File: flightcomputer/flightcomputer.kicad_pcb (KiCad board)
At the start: 4 copper layers, 299 x 188 mm, 69 parts, among them J1 Conn_Coaxial, J10 Conn_01x03, J11 Conn_01x03, J12 ESQ-113-14-G-D, J2 Conn_Coaxial, J3 Conn_Coaxial, J4 Conn_Coaxial, J5 S3B-PH-K-S-GW, J6 S3B-PH-K-S-GW, J7 S4B-PH-K-S_LF__SN_, J8 S3B-PH-K-S-GW, J9 Conn_01x06, U1 MAX-M10S, U2 LIS2MDLTR, U3 BMI088, U4 MS5607-02BA, U7 Teensy4.1, U8 LSM6DSO32TR, U9 RFM96W-433S2

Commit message: resize
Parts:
- added G***: LOGO, HPRlibrary:HPRLOGOSILK, F.Cu at (237.0, 100.0)
- moved C9 102.5 mm to (40.2, 16.8), turned to 0 degrees
- moved U1 91.9 mm to (40.2, 25.8), turned to -90 degrees
- moved R1 84.6 mm to (45.2, 35.7), turned to 90 degrees
- moved R2 81.8 mm to (42.2, 35.8), turned to -90 degrees
- moved TP3 81.4 mm to (50.2, 17.8), turned to 180 degrees
- moved R7 79.3 mm to (39.6, 36.0), turned to -90 degrees
- moved J2 71.3 mm to (45.2, 44.8), turned to -90 degrees
- moved TP2 69.0 mm to (50.2, 28.8), turned to 180 degrees
- moved BT1 67.7 mm to (44.5, 47.8), turned to 180 degrees
- moved J1 61.7 mm to (35.2, 44.8), turned to -90 degrees
- moved R17 53.1 mm to (20.7, 109.2), turned to 180 degrees
- moved J11 51.2 mm to (61.9, 130.0)
- moved S1 44.4 mm to (19.2, 116.2)
- moved J9 31.7 mm to (145.5, 96.0), turned to -90 degrees
- moved TP1 24.1 mm to (131.0, 121.0), turned to 90 degrees
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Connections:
- J12 pad 01: Net-(J12-Pad01) -> GND
- J12 pad 02: /5V -> Net-(J12-Pad02)
- J12 pad 03: Net-(J12-Pad03) -> GND
- J12 pad 04: /5V -> Net-(J12-Pad04)
- J12 pad 05: /aux7_rx -> GND
- J12 pad 06: /5V -> /aux7_rx
- J12 pad 07: /aux7_tx -> GND
- J12 pad 08: /5V -> /aux7_tx
- J12 pad 09: /can_rx -> GND
- J12 pad 10: /5V -> /can_rx
- J12 pad 11: /can_tx -> GND
- J12 pad 12: /5V -> /can_tx
- J12 pad 13: /SENSE_mosi -> /5V
- J12 pad 14: /5V -> /SENSE_mosi
- J12 pad 15: /SENSE_miso -> /5V
- J12 pad 16: GND -> /SENSE_miso
- J12 pad 17: /SENSE_sck -> /5V
- J12 pad 18: GND -> /SENSE_sck
- J12 pad 19: /servo2_pwm -> /5V
- J12 pad 20: GND -> /servo2_pwm
- J12 pad 21: /servo1_pwm -> /5V
- J12 pad 22: GND -> /servo1_pwm
- J12 pad 23: /PYRO1 -> /5V
- J12 pad 24: GND -> /PYRO1
- J12 pad 25: /PYRO2 -> /5V
- J12 pad 26: GND -> /PYRO2
- R15 pad 1: /teensy_3.3v -> Net-(J12-Pad04)
- R15 pad 2: Net-(J12-Pad03) -> /teensy_3.3v
- R16 pad 1: /teensy_3.3v -> Net-(J12-Pad02)
- R16 pad 2: Net-(J12-Pad01) -> /teensy_3.3v
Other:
- board size 299 x 188 mm -> 130 x 70 mm

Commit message: flight computer routing
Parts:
- removed R16: 0, Resistor_SMD:R_0603_1608Metric_Pad0.98x0.95mm_HandSolder
- removed TP15, TP16, TP17, TP18, TP5, TP6, TP7, TP8: TestPoint, Connector_PinHeader_2.54mm:PinHeader_1x01_P2.54mm_Vertical
- added J14: S3B-PH-K-S-GW, HPRlibrary:S3BPHKSGW, F.Cu at (113.0, 70.5)
- added TP1: TestPoint, Connector_PinHeader_2.54mm:PinHeader_1x01_P2.54mm_Vertical, F.Cu at (109.0, 77.0)
- C9: moved to B.Cu
- J6, J8: value S3B-PH-K-S-GW -> Conn_01x03; footprint HPRlibrary:S3BPHKSGW -> Connector_PinHeader_2.54mm:PinHeader_1x03_P2.54mm_Vertical
- moved C9 112.5 mm to (67.0, 126.0)
- moved BT1 87.2 mm to (63.0, 133.0), turned to 0 degrees
- moved U1 86.7 mm to (56.0, 111.0)
- moved R7 86.0 mm to (55.4, 120.5)
- moved J2 85.5 mm to (52.0, 130.0)
- moved TP3 84.8 mm to (61.9, 101.8)
- moved R1 82.0 mm to (66.0, 115.0)
- moved J1 79.6 mm to (43.0, 124.0), turned to 180 degrees
- moved R2 78.9 mm to (66.0, 111.0)
- moved TP2 73.2 mm to (56.0, 101.8)
- moved J6 53.0 mm to (132.0, 75.5), turned to 0 degrees
- moved J9 41.3 mm to (105.5, 106.0), turned to 90 degrees
- moved J10 37.4 mm to (132.0, 100.5), turned to 0 degrees
- moved C10 36.0 mm to (114.0, 111.0), turned to 0 degrees
- moved J12 35.8 mm to (126.0, 75.0)
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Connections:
- J12 pad 01: GND -> Net-(J12-Pad01)
- J12 pad 02: Net-(J12-Pad02) -> unconnected-(J12-Pad02)
- J12 pad 03: GND -> /servo2_pwm
- J12 pad 04: Net-(J12-Pad04) -> unconnected-(J12-Pad04)
- J12 pad 05: GND -> /servo1_pwm
- J12 pad 06: /aux7_rx -> unconnected-(J12-Pad06)
- J12 pad 08: /aux7_tx -> unconnected-(J12-Pad08)
- J12 pad 10: /can_rx -> unconnected-(J12-Pad10)
- J12 pad 12: /can_tx -> unconnected-(J12-Pad12)
- J12 pad 13: /5V -> GND
- J12 pad 14: /SENSE_mosi -> unconnected-(J12-Pad14)
- J12 pad 15: /5V -> GND
- J12 pad 16: /SENSE_miso -> unconnected-(J12-Pad16)
- J12 pad 17: /5V -> GND
- J12 pad 18: /SENSE_sck -> unconnected-(J12-Pad18)
- J12 pad 20: /servo2_pwm -> unconnected-(J12-Pad20)
- J12 pad 22: /servo1_pwm -> unconnected-(J12-Pad22)
- J12 pad 24: /PYRO1 -> unconnected-(J12-Pad24)
- J12 pad 26: /PYRO2 -> unconnected-(J12-Pad26)
- J6 pad 1: /aux2_tx -> GND
- J6 pad 2: /aux2_rx -> GND
- J8 pad 1: /aux7_tx -> /SENSE_mosi
- J8 pad 2: /aux7_rx -> /SENSE_miso
- J8 pad 3: GND -> /SENSE_sck
- J9 pad 1: /radio_dio5 -> /radio_dio3
- J9 pad 3: /radio_dio3 -> /radio_dio5
- J9 pad 4: /radio_dio2 -> /radio_dio1
- J9 pad 5: /radio_dio1 -> /radio_dio2
- R1 pad 1: /gps_3.3v -> /teensy_3.3v
- R15 pad 1: Net-(J12-Pad04) -> /teensy_3.3v
- R15 pad 2: /teensy_3.3v -> Net-(J12-Pad01)
- R2 pad 1: /gps_3.3v -> /teensy_3.3v
- TP4 pad 1: /SENSE_sck -> /can_rx
- U7 pad 10: /aux2_tx -> /PYRO1CONN
- U7 pad 11: /buzz_pwm -> /radio_reset
- U7 pad 16: /imu_accel_int1 -> /x_fault
- U7 pad 17: /imu_gyro_int1 -> /x_cursns
- U7 pad 20: /aux7_rx -> /lsmimu_int
- U7 pad 21: /aux7_tx -> /lsmimu_cs
- U7 pad 24: /radio_reset -> /buzz_pwm
- U7 pad 25: unconnected-(U7-33_MCLK2-Pad25) -> /imu_gyro_int1
- U7 pad 31: unconnected-(U7-39_MISO1_OUT1A-Pad31) -> /imu_accel_int1
- U7 pad 32: /PYRO1 -> /5v_fault
- U7 pad 33: /PYRO2 -> /5v_cursns
- U7 pad 44: /lsmimu_cs -> /6v_fault
- U7 pad 45: /lsmimu_int -> /6v_cursns
- U7 pad 7: unconnected-(U7-5_IN2-Pad7) -> /PYRO2
- U7 pad 8: unconnected-(U7-6_OUT1D-Pad8) -> /PYRO1
- U7 pad 9: /aux2_rx -> /PYRO2CONN
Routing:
- net /SENSE_sck: track 0.00 -> 80.5 mm
- net /radio_sck: track 0.00 -> 61.7 mm, vias 0 -> 1
- net /radio_reset: track 0.00 -> 58.9 mm, vias 0 -> 1
- net /SENSE_mosi: track 0.00 -> 54.9 mm
- net /SENSE_miso: track 0.00 -> 51.0 mm
- net /buzz_pwm: track 0.00 -> 49.3 mm
- net /imu_gyro_int1: track 0.00 -> 47.1 mm, vias 0 -> 1
- net /radio_mosi: track 0.00 -> 40.5 mm, vias 0 -> 1
- net /teensy_3.3v: track 0.00 -> 40.5 mm, vias 0 -> 1
- net /aux1_sda: track 0.00 -> 37.6 mm
- net /imu_gyro_cs: track 0.00 -> 37.1 mm, vias 0 -> 1
- net /imu_accel_cs: track 0.00 -> 33.1 mm, vias 0 -> 1
- net /radio_cs: track 0.00 -> 30.3 mm
- net /aux8_tx: track 0.00 -> 29.5 mm
- net /aux1_scl: track 0.00 -> 29.0 mm
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- added copper zone on B.Cu, net /gps_vbckp
- added copper zone on F.Cu, net /gps_vbckp
- added copper zone on In2.Cu, net /teensy_3.3v
- added copper zone on B.Cu, net GND
- added copper zone on F.Cu, net GND
- added copper zone on In1.Cu, net GND
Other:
- board size 130 x 70 mm -> 100 x 75 mm
- rule pad_to_mask_clearance: 0 -> 0.1

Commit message: fc checkpoint
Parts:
- moved TP4 12.7 mm to (103.5, 71.5)
- moved TP1 11.9 mm to (103.5, 66.5)
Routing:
- net /radio_mosi: track 40.5 -> 61.0 mm, vias 1 -> 2
- net /teensy_3.3v: track 40.5 -> 53.5 mm, vias 1 -> 6
- net /SENSE_mosi: track 54.9 -> 65.3 mm, vias 0 -> 1
- net GND: track 11.5 -> 17.4 mm, vias 0 -> 11
- net /buzz_pwm: track 49.3 -> 52.4 mm
- net /SENSE_sck: track 80.5 -> 81.4 mm
- added copper zone on In2.Cu, net /5V

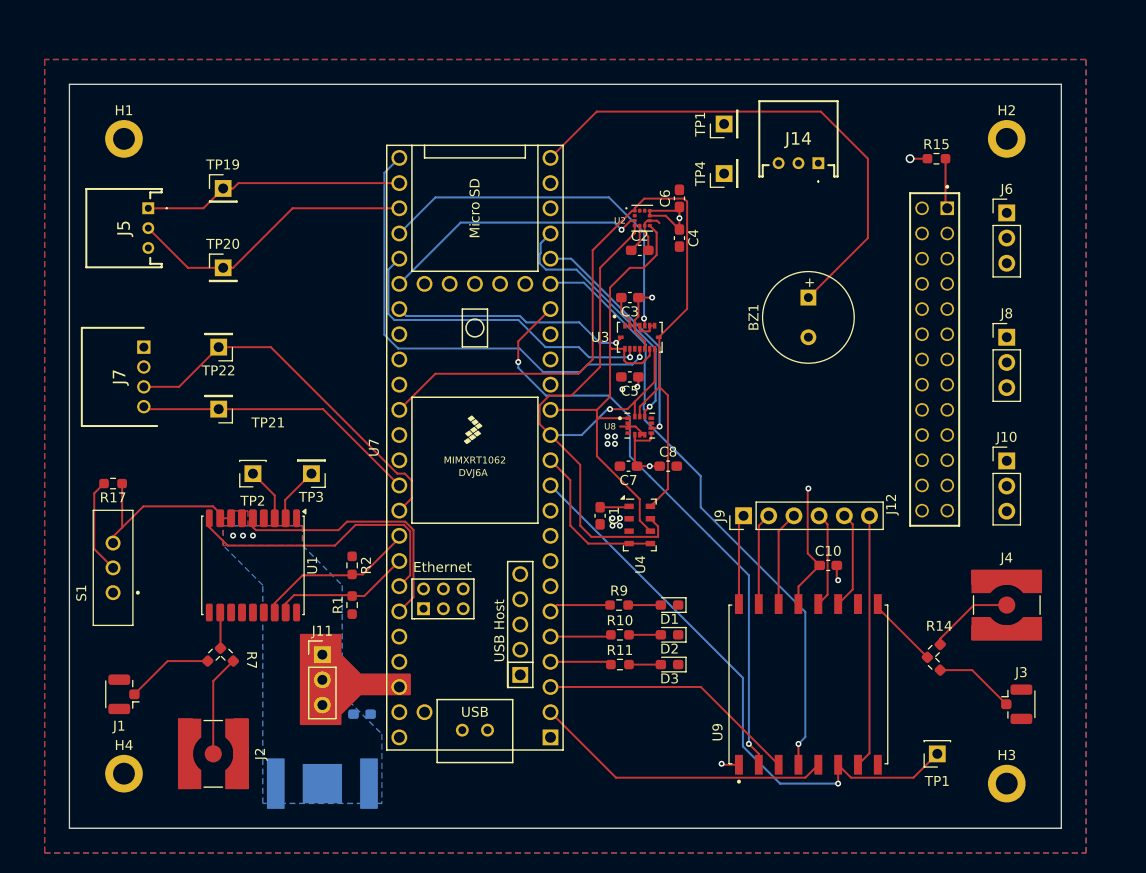
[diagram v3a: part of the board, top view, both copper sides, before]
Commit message: clean up, aligning connectors and board coordinates between fc and power board
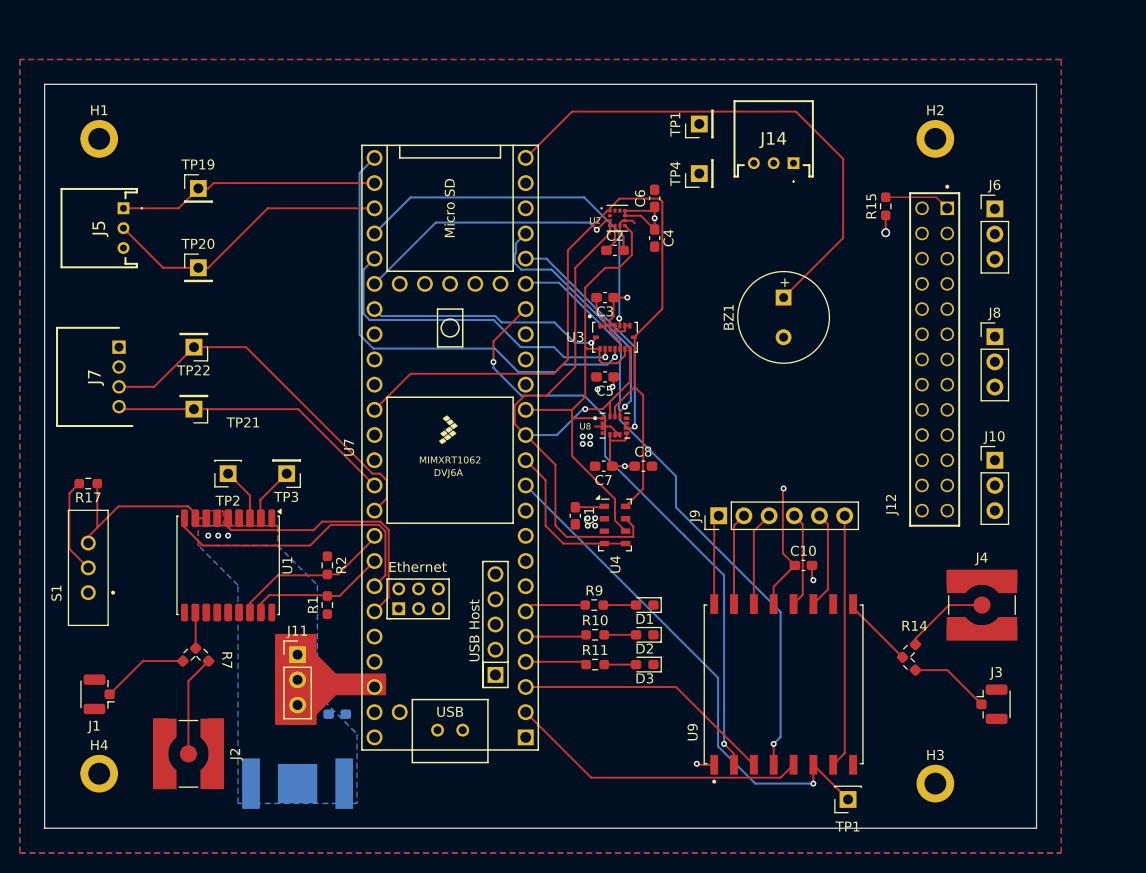
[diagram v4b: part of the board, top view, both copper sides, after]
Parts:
- moved TP1 10.1 mm to (116.0, 134.6)
- moved H2 7.20 mm to (124.8, 68.0)
- moved H3 7.20 mm to (124.8, 133.0)
- moved R15 7.01 mm to (119.8, 74.8), turned to 90 degrees
- moved BT1 2.50 mm to (60.5, 133.0)
- moved BZ1 2.50 mm to (109.5, 84.0)
- moved C1 2.50 mm to (88.5, 106.0)
- moved C10 2.50 mm to (111.5, 111.0)
- moved C2 2.50 mm to (92.5, 79.2)
- moved C3 2.50 mm to (91.5, 84.0)
- moved C4 2.50 mm to (96.5, 78.0)
- moved C5 2.50 mm to (91.5, 92.0)
- moved C6 2.50 mm to (96.5, 74.0)
- moved C7 2.50 mm to (91.4, 101.0)
- moved C8 2.50 mm to (95.4, 101.0)
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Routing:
- net /radio_reset: track 58.9 -> 52.3 mm
- net Net-(J12-Pad01): track 5.07 -> 6.66 mm

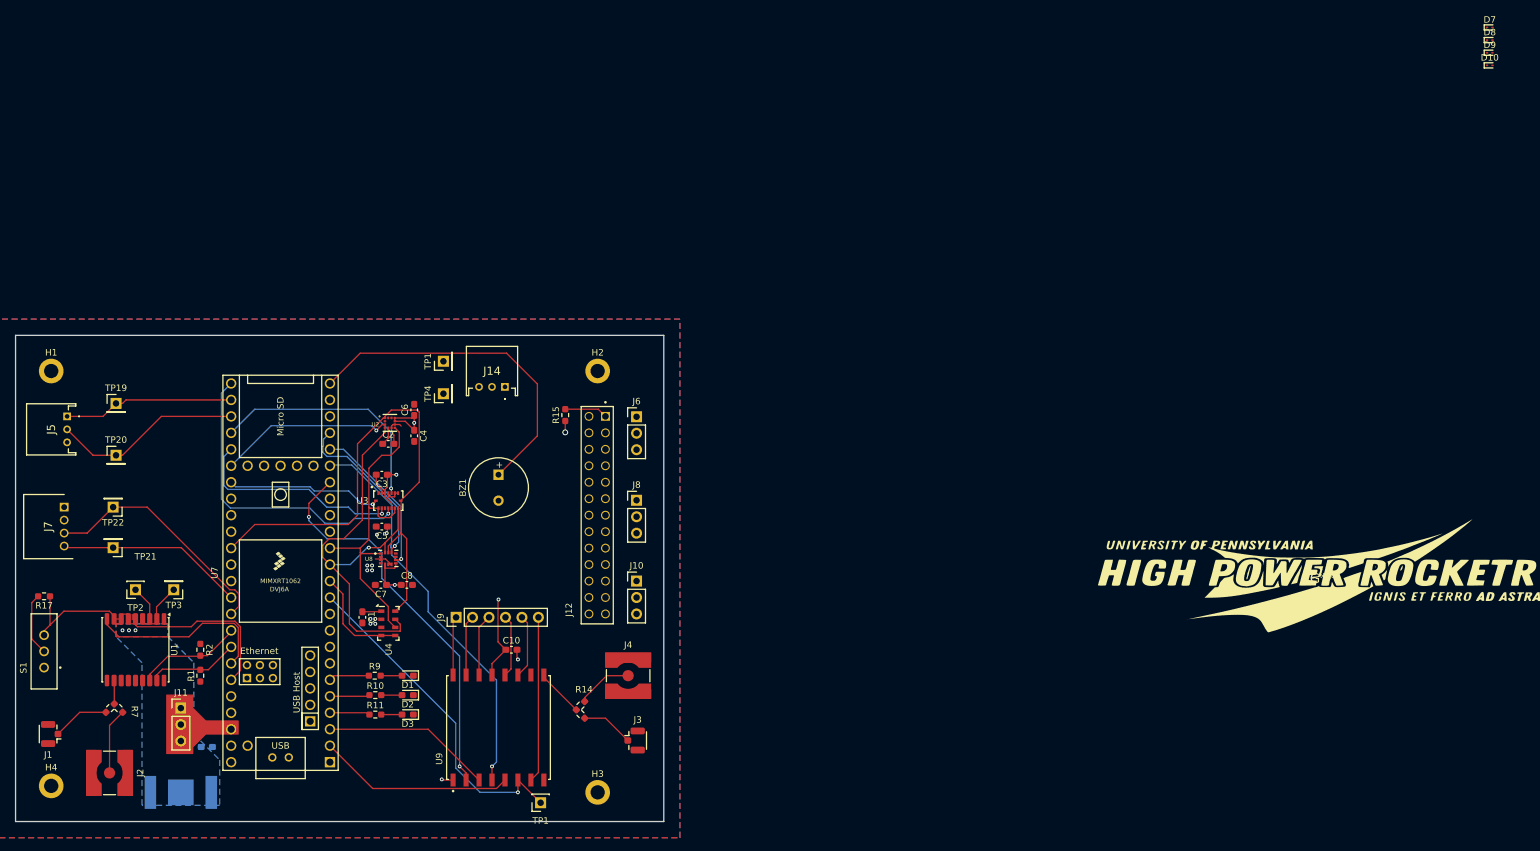
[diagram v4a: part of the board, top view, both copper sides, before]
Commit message: hole+connector alignment finish, fc signal routing finish, fc drc warnings related to footprints/silkscreen
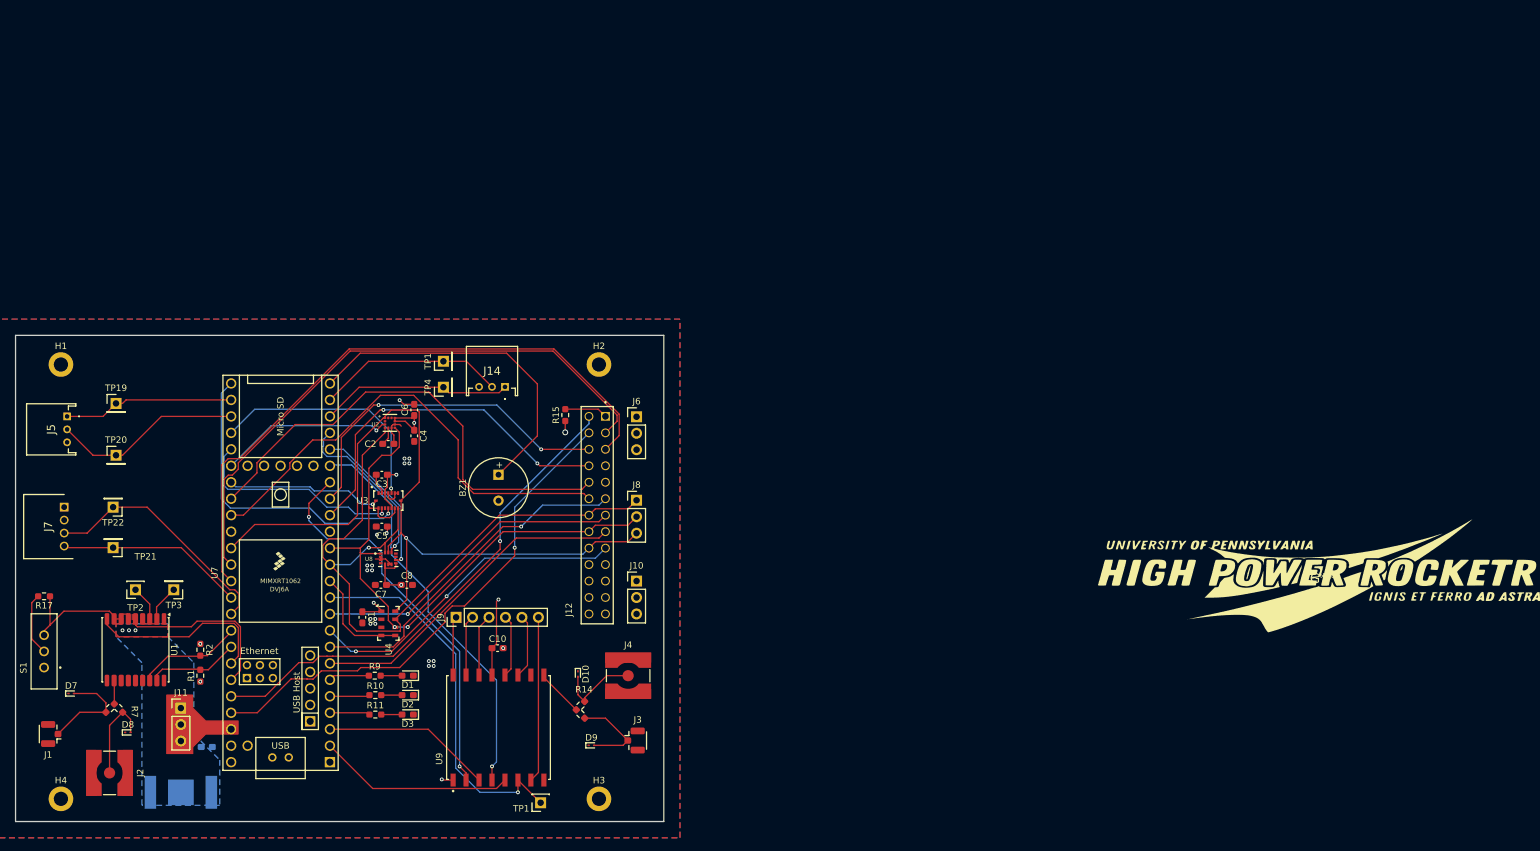
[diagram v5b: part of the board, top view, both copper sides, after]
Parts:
- moved D7 241.8 mm to (43.6, 117.8)
- moved D8 235.7 mm to (52.3, 123.8)
- moved D9 175.0 mm to (123.8, 125.8)
- moved D10 169.1 mm to (121.8, 114.8), turned to -90 degrees
- moved H4 2.50 mm to (42.0, 134.0)
- moved C10 2.15 mm to (109.4, 110.8)
- moved H1 1.80 mm to (42.0, 67.0)
- moved H2 1.02 mm to (125.0, 67.0)
- moved H3 1.02 mm to (125.0, 134.0)
- moved TP4 1.00 mm to (101.0, 70.5)
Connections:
- J12 pad 02: unconnected-(J12-Pad02) -> /6v_fault
- J12 pad 04: unconnected-(J12-Pad04) -> /6v_cursns
- J12 pad 06: unconnected-(J12-Pad06) -> /x_cursns
- J12 pad 07: GND -> unconnected-(J12-Pad07)
- J12 pad 08: unconnected-(J12-Pad08) -> /x_fault
- J12 pad 09: GND -> unconnected-(J12-Pad09)
- J12 pad 10: unconnected-(J12-Pad10) -> /5v_fault
- J12 pad 11: GND -> /PYRO1
- J12 pad 12: unconnected-(J12-Pad12) -> /5v_cursns
- J12 pad 13: GND -> /PYRO1CONN
- J12 pad 14: unconnected-(J12-Pad14) -> /SENSE_mosi
- J12 pad 15: GND -> /PYRO2
- J12 pad 16: unconnected-(J12-Pad16) -> /SENSE_miso
- J12 pad 17: GND -> /PYRO2CONN
- J12 pad 18: unconnected-(J12-Pad18) -> /SENSE_sck
- J12 pad 20: unconnected-(J12-Pad20) -> GND
- J12 pad 22: unconnected-(J12-Pad22) -> GND
- J12 pad 24: unconnected-(J12-Pad24) -> GND
- J12 pad 26: unconnected-(J12-Pad26) -> GND
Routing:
- net /servo1_pwm: track 0.00 -> 97.7 mm
- net /servo2_pwm: track 0.00 -> 90.6 mm
- net /6v_cursns: track 0.00 -> 78.3 mm, vias 0 -> 1
- net /6v_fault: track 0.00 -> 77.5 mm, vias 0 -> 1
- net /5v_fault: track 0.00 -> 74.4 mm
- net /5v_cursns: track 0.00 -> 73.7 mm
- net /x_fault: track 0.00 -> 55.2 mm, vias 0 -> 2
- net /x_cursns: track 0.00 -> 53.3 mm, vias 0 -> 2
- net /PYRO1: track 0.00 -> 52.9 mm, vias 0 -> 1
- net /PYRO2: track 0.00 -> 50.9 mm
- net /PYRO2CONN: track 0.00 -> 50.5 mm, vias 0 -> 2
- net /PYRO1CONN: track 0.00 -> 48.8 mm, vias 0 -> 1
- net /SENSE_mosi: track 65.3 -> 110.1 mm
- net /SENSE_miso: track 51.0 -> 95.4 mm, vias 0 -> 2
- net /SENSE_sck: track 81.4 -> 119.4 mm, vias 0 -> 1
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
